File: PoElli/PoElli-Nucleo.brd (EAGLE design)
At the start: 79.5 x 70 mm, 121 parts, among them CN10 NUCLEO-CN10, CN7 NUCLEO-CN7, J3 M022.54MM, J4 M022.54MM, Q3 FDMC2674, Q4 IRFL4310, SW1 A6H2101, SW2 A6H2101, T1 Coilcraft 230NL, T2 FLYBACK750311689, U4 LT3748, U5 TPS2378, U6 ENC424J600, X1 POE-TP-SHIELDED-RJ45-MOLEX-85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, Y1 25 MHz

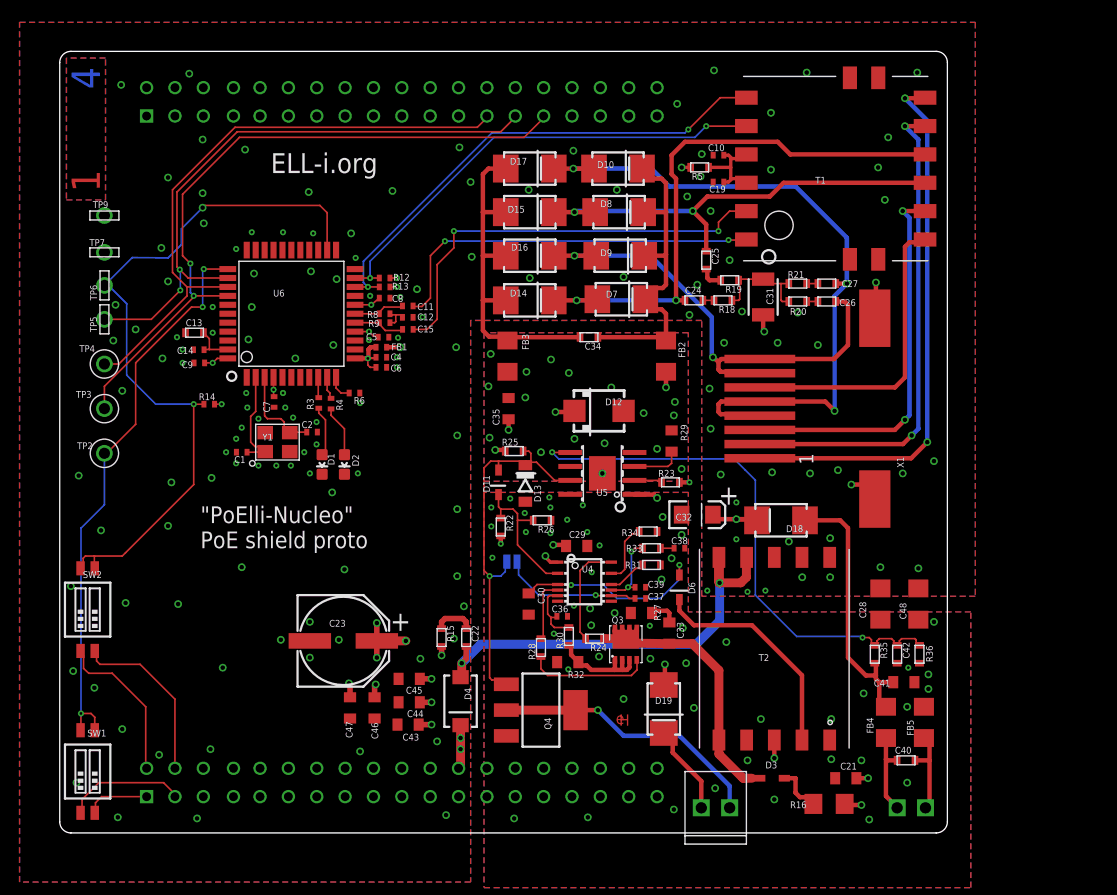
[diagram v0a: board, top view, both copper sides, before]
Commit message: Fix mistakes from first prototype round
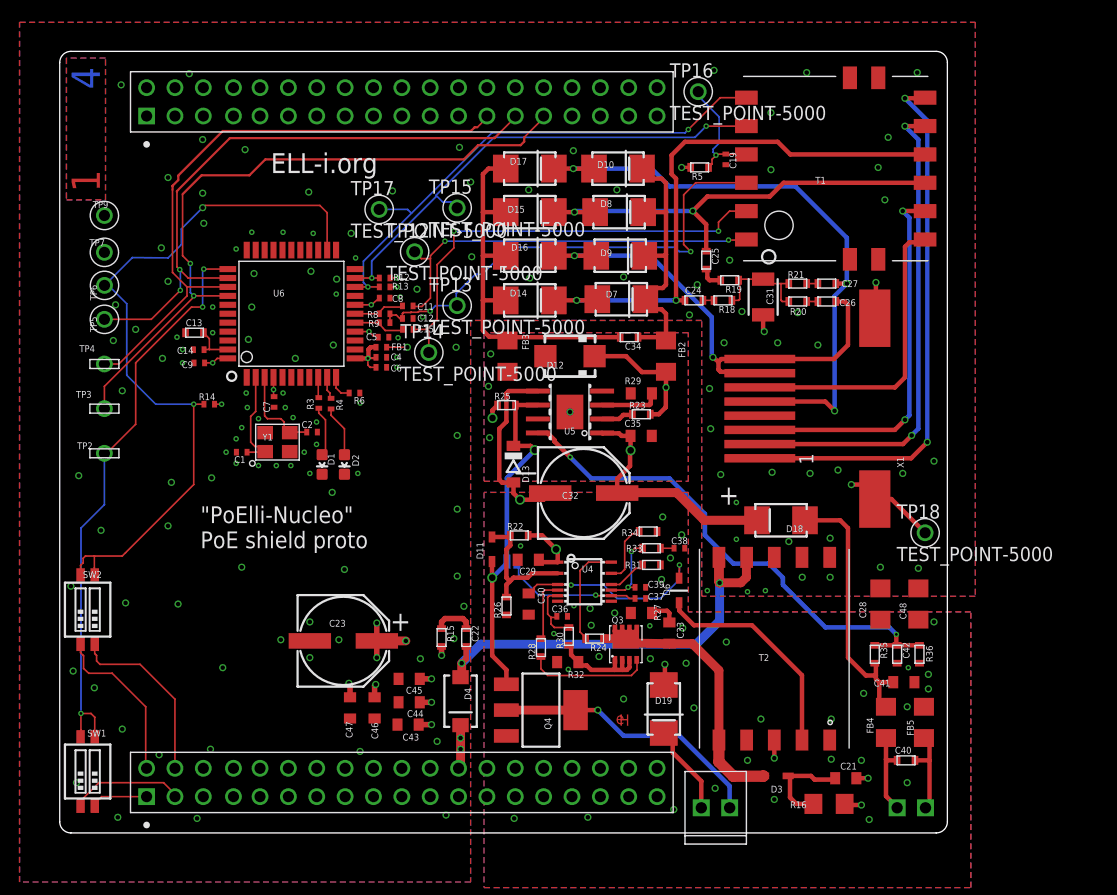
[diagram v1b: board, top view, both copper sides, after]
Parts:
- removed C10: 10nF, ELL-i-Passives:C0402
- added TP12, TP13, TP14, TP15, TP16, TP17, TP18: TEST_POINT-5000, ELL-i-Passives:TP_5000
- C12: value 100nF -> 10nF
- C32: value 47uF -> 10uF 100 V; device ELL-i-Passives:CT3216 -> ELL-i-Passives:CPOL_PANASONIC_E
- CN7: value NUCLEO-CN7 -> NUCLEO-CN10
- TP2, TP3, TP4: device ELL-i-Passives:TP_5000 -> ELL-i-Passives:TP_5021
- TP5, TP6, TP7, TP9: device ELL-i-Passives:TP_5021 -> ELL-i-Passives:TP_5000
- moved C35 12.1 mm to (52.1, 35.6), turned to 0 degrees
- moved C32 10.4 mm to (46.9, 30.4)
- moved R26 8.31 mm to (40.0, 20.3), turned to 90 degrees
- moved R23 6.64 mm to (52.1, 37.5)
- moved U5 6.22 mm to (45.7, 37.7)
- moved D11 6.02 mm to (38.7, 25.4)
- moved D12 5.55 mm to (45.7, 42.7), turned to 180 degrees
- moved R29 5.06 mm to (52.1, 39.4), turned to 0 degrees
- moved C29 4.51 mm to (42.0, 24.5), turned to 180 degrees
- moved R25 4.17 mm to (40.0, 38.3)
- moved C34 3.60 mm to (51.0, 44.4)
- moved C19 2.13 mm to (59.7, 60.3), turned to 90 degrees
- moved D13 2.03 mm to (40.6, 33.0)
- moved R22 1.82 mm to (41.2, 26.6), turned to 0 degrees
- moved D3 0.40 mm to (64.1, 5.11), turned to 180 degrees
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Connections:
- removed net N$44: C12.2, R8.1, R9.1
- new net TPINCT: C12.2, R8.1, R9.1, T1.3, TP13.P$1
- net GNDA: no longer C10.1
- net INTVCC: now also D6.C; no longer D6.2
- net N$28: now also D3.A; no longer D3.1
- net N$29: now also D6.A; no longer D6.1
- net N$33: now also D3.C; no longer D3.2
- net N$40: now also TP16.P$1; no longer C10.2, T1.3
- net N$54: now also U5.8; no longer U5.5
- net RTN: now also C32.-, U5.5; no longer C32.C, U5.8
- net SGND: now also TP18.P$1
- net TPIN+: now also TP14.P$1
- net TPIN-: now also TP12.P$1
- net TPOUT+: now also TP17.P$1
- net TPOUT-: now also TP15.P$1
- net U4_EN: now also D11.A; no longer D11.1
- net U5_CDB: now also D11.C, U5.6; no longer D11.2, U5.7
- net VDD: now also C32.+; no longer C32.A
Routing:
- net TPINCT: track 0.00 -> 43.3 mm, vias 0 -> 2
- net VDD: track 24.6 -> 46.7 mm, vias 14 -> 8
- net RTN: track 0.00 -> 17.0 mm, vias 50 -> 38
- net POE_B+: track 63.4 -> 55.1 mm
- net SGND: track 34.7 -> 40.5 mm
- net N$33: track 4.35 -> 8.73 mm
- net N$8: track 31.7 -> 35.3 mm
- net N$6: track 29.6 -> 26.0 mm
- net N$54: track 49.5 -> 46.2 mm
- net N$28: track 27.7 -> 24.5 mm
- net TPOUT+: track 45.0 -> 48.0 mm
- net U5_CDB: track 35.1 -> 32.3 mm, vias 1 -> 2
- net N$44: track 2.46 -> 0.00 mm
- net N$40: track 8.72 -> 11.1 mm, vias 0 -> 1
- net TPOUT-: track 42.4 -> 44.7 mm
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
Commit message: rev 3 DRC ok
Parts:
- removed TP12, TP13, TP14, TP15, TP16, TP17: TEST_POINT-5000, ELL-i-Passives:TP_5000
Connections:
- net N$40: no longer TP16.P$1
- net TPIN+: no longer TP14.P$1
- net TPIN-: no longer TP12.P$1
- net TPINCT: no longer TP13.P$1
- net TPOUT+: no longer TP17.P$1
- net TPOUT-: no longer TP15.P$1
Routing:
- net POE_B+: track 55.1 -> 61.9 mm
- net N$40: track 11.1 -> 4.28 mm, vias 1 -> 0
- net N$28: track 24.5 -> 29.5 mm
- net TPOUT+: track 48.0 -> 45.0 mm
- net TPOUT-: track 44.7 -> 42.3 mm
- net TPIN+: track 40.6 -> 38.7 mm
- net TPIN-: track 36.3 -> 34.6 mm
- net VDD: track 46.7 -> 47.6 mm
- net TPINCT: track 43.3 -> 42.6 mm

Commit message: rev 0.3
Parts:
- Q3: value FDMC2674 -> FDMC2674HANDSOLDERING; device ELL-i-DIscreteSemi:MLP8L33 -> ELL-i-DIscreteSemi:MLP8L33_HS
- moved C25 2.08 mm to (56.9, 49.5), turned to 0 degrees
- moved Q3 0.44 mm to (50.7, 16.5)
- moved C5 0.21 mm to (28.8, 44.5)
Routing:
- net RTN: track 17.0 -> 94.4 mm, vias 38 -> 11
- net GNDA: track 0.00 -> 48.5 mm, vias 137 -> 24
- net +3V3: track 4.12 -> 34.4 mm, vias 4 -> 3
- net U4_SS: track 12.6 -> 38.9 mm
- net POE_A+: track 50.6 -> 75.1 mm
- net VDD: track 47.6 -> 70.0 mm
- net POE_B+: track 61.9 -> 80.3 mm, vias 3 -> 2
- net POE_A-: track 40.4 -> 52.5 mm
- net VIN: track 16.2 -> 28.3 mm, vias 11 -> 0
- net N$8: track 35.3 -> 25.7 mm
- net UNREG_6V+: track 41.3 -> 33.7 mm
- net N$6: track 26.0 -> 18.7 mm
- net ENC-3V3: track 15.0 -> 21.9 mm, vias 6 -> 5
- net ETH_SS: track 52.5 -> 59.3 mm, vias 3 -> 0
- net SGND: track 40.5 -> 47.0 mm
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- removed copper zone on layer 2, net VSS
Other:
- board text added: "2014-07-21"
- board text added: "PoElli-Nucleo PoE shield proto rev 0.3"
- board text removed: ""PoElli-Nucleo" PoE shield proto"

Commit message: PoElli 0.4 Schema, tentative layout
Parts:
- removed C14: 100nF, ELL-i-Passives:C0402
- removed C23: 220uF, ELL-i-Passives:CPOL_PANASONIC_E
- removed C29: 1uF, ELL-i-Passives:C0805
- removed CN10, CN7: NUCLEO-CN10, ELL-i-Boards:NUCLEO-HEADER
- removed NUCLEO: NUCLEO-SHIELD-OUTLINE-EXTENDED, ELL-i-Boards:NUCLEO-SHIELD-UNDERSIDE-EXTENDED-OUTLINE
- removed R38: OPEN, SparkFun-Passives:SJ_2S-NO
- removed SW1, SW2: A6H2101, SparkFun-Electromechanical:DIPSWITCH-02-50MIL
- removed T2: FLYBACK750311689, ELL-i-Transformers:WE_EP13_SMD_10PIN
- added SJ1, SJ2, SJ3, SJ4: SOLDERJUMPERNO, SparkFun-Passives:SJ_2S-NO
- added U$2: NUCLEO-SHIELD-20PIN, ELL-i-Boards:NUCLEO-SHIELD-UNDERSIDE-SHORT-20-PINHEADER
- C1, C12, C19, C2, C36, C37, C38, C39: device ELL-i-Passives:C0402 -> ELL-i-Passives:SMD0805-A
- C13, C22, C42: device ELL-i-Passives:C0603 -> ELL-i-Passives:SMD0805-A
- C24, C25, C26, C27: value 10nF -> 10nF 100V; device ELL-i-Passives:C0603 -> ELL-i-Passives:SMD0805-A
- C28, C48: value 1nF -> 1nF 2kV
- C30: value 4u7 -> 4u7 25 V; device ELL-i-Passives:C0805 -> ELL-i-Passives:SMD0805-A
- C31: value 1nF -> 1nF 2kV; device ELL-i-Passives:C1210 -> ELL-i-Passives:SMD1206-A
- C32: device ELL-i-Passives:CPOL_PANASONIC_E -> ELL-i-Passives:SMD1206-A
- C33: value 150pF NP -> 150pF 200V NP; device ELL-i-Passives:C0805 -> ELL-i-Passives:SMD0805-A
- C34, C40: value 1nF -> 10nF 100V; device ELL-i-Passives:C0603 -> ELL-i-Passives:SMD0402-B
- C35, C41: value 100nF -> 100nF 100V; device ELL-i-Passives:C0805 -> ELL-i-Passives:SMD0805-A
- C4: value 47pF -> 100nF; device ELL-i-Passives:C0402 -> ELL-i-Passives:SMD0805-A
- C43, C44, C45, C46, C47: device ELL-i-Passives:C0805 -> ELL-i-Passives:SMD1206-A
- C5, C6, C7: value 1nF -> 100nF; device ELL-i-Passives:C0402 -> ELL-i-Passives:SMD0805-A
- C8, C9: device ELL-i-Passives:C0402 -> ELL-i-Passives:SMD0402-B
- D2: value YELLOW -> GREEN
- Q4: value IRFL4310 -> FDMC2674HANDSOLDERING; device ELL-i-DIscreteSemi:SOT223 -> ELL-i-DIscreteSemi:MLP8L33_HS
- R12, R13, R14, R6, R8, R9: device ELL-i-Passives:R0402 -> ELL-i-Passives:SMD0805-A
- R15, R18, R19, R20, R21, R24, R28, R30, R31, R33, R34, R35, R36: device ELL-i-Passives:R0603 -> ELL-i-Passives:SMD0805-A
- R27: device ELL-i-Passives:R0805 -> ELL-i-Passives:SMD0805-A
- R3, R4: value 180 -> 220; device ELL-i-Passives:R0402 -> ELL-i-Passives:SMD0805-A
- U$1: value (none) -> FLYBACK-3_OUTPUTS_749119350; device hapines:EH-LOGO -> ELL-i-Transformers:WE_749119350
- X1: value POE-TP-SHIELDED-RJ45-MOLEX-85502-5008 -> POE-TP-SHIELDED-LEDSTE1888250; device ELL-i-Connectors:MOLEX-85502-5008 -> ELL-i-Connectors:TE1888250
- moved C48 206.8 mm to (-110.5, 108.0), turned to 0 degrees
- moved R36 199.7 mm to (-86.4, 130.8), turned to 0 degrees
- moved C28 199.1 mm to (-105.4, 108.0), turned to 0 degrees
- moved TP18 194.3 mm to (-99.1, 108.0)
- moved C42 191.4 mm to (-80.0, 128.3), turned to 0 degrees
- moved R35 191.3 mm to (-80.0, 130.8), turned to 0 degrees
- moved J4 189.7 mm to (-82.5, 108.0), flipped to the top, turned to 0 degrees
- moved R18 189.2 mm to (-111.8, 128.3), turned to 0 degrees
- moved C41 188.3 mm to (-73.7, 128.3)
- moved C40 187.9 mm to (-67.3, 128.3)
- moved C25 186.8 mm to (-114.3, 124.5)
- moved C24 181.8 mm to (-108.0, 124.5)
- moved J3 172.4 mm to (-76.2, 108.0), turned to 0 degrees
- moved C19 167.7 mm to (-95.2, 124.5), turned to 0 degrees
- moved D3 165.0 mm to (-58.4, 115.6), turned to 0 degrees
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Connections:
- removed net UNREG_6V+: C22.2, D4.A, T2.6, T2.7
- new net TRAFO_OUT: C22.P$2, D4.A, U$1.P$10, U$1.P$11, U$1.P$12
- net +3V3: now also R12.P$2, R13.P$2, U$2.CN7_12, U$2.CN7_16; no longer CN7.12, CN7.16, R12.2, R13.2
- net ENC-3V3: now also C4.P$2, C5.P$2, C6.P$2, C7.P$2, R14.P$2; no longer C4.2, C5.2, C6.2, C7.2, R14.2
- net ETH_INT: now also R14.P$1, SJ1.1, SJ2.1; no longer R14.1, SW2.3, SW2.4
- net ETH_MISO: now also U$2.CN10_27; no longer CN10.27
- net ETH_MOSI: now also U$2.CN10_25; no longer CN10.25
- net ETH_SCK: now also U$2.CN10_29; no longer CN10.29
- net ETH_SS: now also SJ3.1, SJ4.1; no longer SW1.3, SW1.4
- net GNDA: now also C1.P$2, C12.P$1, C13.P$2, C19.P$1, C2.P$2, C4.P$1, C43.P$2, C44.P$2, C45.P$2, C46.P$2, C47.P$2, C5.P$1, C6.P$1, C7.P$1, R6.P$1, U$1.P$7, U$1.P$8, U$1.P$9, U$2.CN7_22; no longer C1.2, C12.1, C13.2, C14.2, C19.1, C2.2, C23.-, C4.1, C43.2, C44.2, C45.2, C46.2, C47.2, C5.1, C6.1, C7.1, CN7.22, R6.1, T2.10, T2.9
- net INTVCC: now also C30.P$1; no longer C30.1
- net N$10: now also Q4.5, Q4.6, Q4.7, Q4.8, Q4.F1; no longer Q4.2, Q4.4
- net N$11: now also SJ3.2, U$2.CN7_1; no longer CN7.1, SW1.2
- net N$12: now also SJ4.2, U$2.CN7_3; no longer CN7.3, SW1.1
- net N$13: now also SJ2.2, U$2.CN7_2; no longer CN7.2, SW2.1
- net N$14: now also SJ1.2, U$2.CN7_4; no longer CN7.4, SW2.2
- net N$15: now also C33.P$2, R27.P$1; no longer C33.2, R27.1
- net N$16: now also C22.P$1, R15.P$1; no longer C22.1, R15.1
- net N$22: now also C39.P$1, R33.P$2; no longer C39.1, R33.2
- net N$23: now also C38.P$1, R33.P$1; no longer C38.1, R33.1
- net N$24: now also R28.P$2; no longer R28.2
- net N$25: now also R28.P$1; no longer R28.1
- net N$26: now also C36.P$1, R30.P$2; no longer C36.1, R30.2
- net N$27: now also R30.P$1; no longer R30.1
- net N$28: now also C33.P$1, R24.P$1, U$1.P$1; no longer C33.1, R24.1, T2.5
- net N$29: now also U$1.P$5; no longer T2.2
- net N$31: now also R24.P$2; no longer R24.2
- net N$32: now also R34.P$2; no longer R34.2
- net N$36: now also R4.P$2; no longer R4.2
- net N$37: now also C1.P$1; no longer C1.1
- net N$38: now also R3.P$1; no longer R3.1
- net N$39: now also R8.P$2; no longer R8.2
- net N$40: now also C19.P$2; no longer C19.2
- net N$41: now also R4.P$1; no longer R4.1
- net N$42: now also R3.P$2; no longer R3.2
- net N$45: now also R6.P$2; no longer R6.2
- net N$47: now also C2.P$1; no longer C2.1
- net N$48: now also C27.P$2, R21.P$2; no longer C27.2, R21.2
- net N$5: now also C31.P$1, R18.P$1, R19.P$1, R20.P$1, R21.P$1; no longer C31.1, R18.1, R19.1, R20.1, R21.1
- net N$50: now also C24.P$2, R18.P$2; no longer C24.2, R18.2
- net N$51: now also C25.P$2, R19.P$2; no longer C25.2, R19.2
- net N$52: now also C26.P$2, R20.P$2; no longer C26.2, R20.2
- net N$54: now also C42.P$1, R35.P$1, R36.P$2; no longer C42.1, R35.1, R36.2
- net N$59: now also R9.P$2; no longer R9.2
- net N$7: now also R31.P$2; no longer R31.2
- net N$76: now also C41.P$1, R35.P$2; no longer C41.1, R35.2
- net POE_A+: now also C24.P$1; no longer C24.1
- net POE_A-: now also C25.P$1; no longer C25.1
- net POE_B+: now also C27.P$1; no longer C27.1
- net POE_B-: now also C26.P$1; no longer C26.1
- net RTN: now also C30.P$2, C32.P$2, C36.P$2, C37.P$2, C38.P$2, C39.P$2, C41.P$2, C42.P$2, Q4.1, Q4.2, R27.P$2, R31.P$1, R34.P$1, R36.P$1, U$1.P$6; no longer C29.2, C30.2, C32.-, C36.2, C37.2, C38.2, C39.2, C41.2, C42.2, R27.2, R31.1, R34.1, R36.1, T2.1
- net SGND: now also C31.P$2, X1.GND@1, X1.GND@2, X1.GND@3, X1.GND@4; no longer C31.2, X1.S1, X1.S2
- net TPINCT: now also C12.P$2, R8.P$1, R9.P$1; no longer C12.2, R8.1, R9.1
- net TPOUT+: now also R13.P$1; no longer R13.1
- net TPOUT-: now also R12.P$1; no longer R12.1
- net U4_SS: now also C37.P$1; no longer C37.1, R38.1
- net U5_CDB: now also Q4.4; no longer Q4.1, R38.2
- net VCAP: now also C13.P$1; no longer C13.1, C14.1
- net VDD: now also C32.P$1, C35.P$1, D12.C, U$1.P$3; no longer C29.1, C32.+, C35.1, D12.1, T2.3
- net VIN: now also C43.P$1, C44.P$1, C45.P$1, C46.P$1, C47.P$1, R15.P$2, U$2.CN7_24; no longer C23.+, C43.1, C44.1, C45.1, C46.1, C47.1, CN7.24, R15.2
- net VSS: now also C35.P$2, D12.A; no longer C35.2, D12.2
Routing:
- net RTN: track 94.4 -> 0.00 mm, vias 11 -> 0
- net POE_B+: track 80.3 -> 0.00 mm, vias 2 -> 0
- net POE_A+: track 75.1 -> 0.00 mm, vias 2 -> 0
- net VDD: track 70.0 -> 0.00 mm, vias 8 -> 0
- net ETH_INT: track 65.8 -> 0.00 mm
- net ETH_SS: track 59.3 -> 0.00 mm
- net ETH_SCK: track 58.3 -> 0.00 mm, vias 1 -> 0
- net POE_A-: track 52.5 -> 0.00 mm, vias 2 -> 0
- net ETH_MOSI: track 51.7 -> 0.00 mm, vias 1 -> 0
- net N$54: track 51.5 -> 0.00 mm, vias 2 -> 0
- net ETH_MISO: track 49.8 -> 0.00 mm, vias 1 -> 0
- net SGND: track 47.0 -> 0.00 mm, vias 3 -> 0
- net POE_B-: track 45.5 -> 0.00 mm, vias 2 -> 0
- net GNDA: track 48.5 -> 3.84 mm, vias 24 -> 0
- net TPINCT: track 39.4 -> 0.00 mm, vias 2 -> 0
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- removed copper zone on layer 15, net +3V3
- removed copper zone on layer 15, net ENC-3V3
- removed copper zone on layer 1, net GNDA
- removed copper zone on layer 16, net GNDA
- removed copper zone on layer 2, net GNDA
- removed copper zone on layer 1, net N$199
- removed copper zone on layer 15, net N$199
- removed copper zone on layer 16, net N$199
- removed copper zone on layer 2, net N$199
- removed copper zone on layer 1, net RTN
- removed copper zone on layer 16, net RTN
- removed copper zone on layer 2, net RTN
- removed copper zone on layer 15, net VDD
- removed copper zone on layer 15, net VIN
- removed copper zone on layer 1, net VSS
- removed copper zone on layer 16, net VSS
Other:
- board size 79.5 x 70 mm -> 160 x 100 mm
- board text removed: "+"
- board text removed: "1"
- board text removed: "2"
- board text removed: "2014-07-21"
- board text removed: "3"
- board text removed: "4"
- board text removed: "ELL-i.org"
- board text removed: "PoElli-Nucleo PoE shield proto rev 0.3"
- board text removed: "https://github.com/Ell-i/ELL-i-Eagle-Boards"

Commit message: tentative layout
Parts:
- removed D10, D14, D15, D16, D17, D7, D8, D9: B2100, ELL-i-DIscreteSemi:DIODE-B2100
- added C10: 1nF 2kV, ELL-i-Passives:SMD1206-A
- added C3: 100nF, ELL-i-Passives:SMD0805-A
- added U$3, U$4: BRIDGE-RECTIFIER, ELL-i-DIscreteSemi:MBS1
- C11, C15: device ELL-i-Passives:C0402 -> ELL-i-Passives:SMD0402-B
- C34: device ELL-i-Passives:SMD0402-B -> ELL-i-Passives:SMD0805-A
- R23, R5: device ELL-i-Passives:R0603 -> ELL-i-Passives:SMD0805-A
- R29: device ELL-i-Passives:R0805 -> ELL-i-Passives:SMD0805-A
- moved R18 211.8 mm to (77.6, 33.5), turned to 90 degrees
- moved C25 208.5 mm to (75.2, 37.5), turned to 270 degrees
- moved C24 204.9 mm to (77.6, 37.5), turned to 270 degrees
- moved J4 203.3 mm to (107.5, 35.5), turned to 270 degrees
- moved J3 195.2 mm to (107.5, 41.7), turned to 270 degrees
- moved C19 190.9 mm to (85.1, 62.0), turned to 270 degrees
- moved D13 177.4 mm to (97.8, 32.8), turned to 270 degrees
- moved FB5 168.4 mm to (101.5, 31.4), turned to 180 degrees
- moved C35 166.5 mm to (95.2, 43.8)
- moved C12 165.7 mm to (70.3, 60.6), turned to 270 degrees
- moved FB4 162.7 mm to (101.4, 33.9), turned to 180 degrees
- moved D12 161.0 mm to (90.9, 31.7), turned to 180 degrees
- moved R29 160.0 mm to (89.5, 39.3)
- moved C31 156.6 mm to (81.5, 31.5)
- moved D18 156.1 mm to (117.5, 44.5), turned to 90 degrees
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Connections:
- new net N$9: C10.P$1, R20.P$1, R21.P$1
- net +3V3: now also R5.P$2; no longer R5.2
- net ENC-3V3: now also C3.P$2
- net GNDA: now also C3.P$1
- net N$18: now also R23.P$1; no longer R23.1
- net N$19: now also R29.P$2; no longer R29.2
- net N$40: now also R5.P$1; no longer R5.1
- net N$5: no longer R20.P$1, R21.P$1
- net N$6: now also C34.P$1, U$3.+, U$4.+; no longer C34.1, D10.C, D7.C, D8.C, D9.C
- net N$8: now also C34.P$2, U$3.-, U$4.-; no longer C34.2, D14.A, D15.A, D16.A, D17.A
- net POE_A+: now also U$3.AC1; no longer D14.C, D7.A
- net POE_A-: now also U$3.AC2; no longer D15.C, D8.A
- net POE_B+: now also U$4.AC1; no longer D10.A, D17.C
- net POE_B-: now also U$4.AC2; no longer D16.C, D9.A
- net SGND: now also C10.P$2
- net VDD: now also R23.P$2; no longer R23.2
- net VSS: now also R29.P$1; no longer R29.1
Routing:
- net POE_B-: track 0.00 -> 33.6 mm
- net POE_B+: track 0.00 -> 19.7 mm
- net TPOUT+: track 18.8 -> 5.02 mm
- net GNDA: track 3.84 -> 15.8 mm
- net TPOUT-: track 12.9 -> 2.18 mm
- net POE_A+: track 0.00 -> 9.43 mm
- net POE_A-: track 0.00 -> 9.00 mm
- net N$59: track 0.00 -> 7.17 mm
- net N$5: track 0.00 -> 6.67 mm
- net N$39: track 0.00 -> 6.49 mm
- net N$9: track 0.00 -> 5.43 mm
- net VIN: track 4.16 -> 0.00 mm
- net TRAFO_OUT: track 4.01 -> 0.00 mm
- net ENC-3V3: track 12.1 -> 15.8 mm
- net N$52: track 0.00 -> 2.08 mm
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
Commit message: Layout, functional blocks placed down
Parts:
- removed U$1: FLYBACK-3_OUTPUTS_749119350, ELL-i-Transformers:WE_749119350
- removed U$3, U$4: BRIDGE-RECTIFIER, ELL-i-DIscreteSemi:MBS1
- added B1, B2: BRIDGE-RECTIFIER, ELL-i-DIscreteSemi:MBS1
- added T2: FLYBACK-3_OUTPUTS_749119350, ELL-i-Transformers:WE_749119350
- C11, C15: device ELL-i-Passives:SMD0402-B -> ELL-i-Passives:SMD0805-A
- C21: device ELL-i-Passives:C0805 -> ELL-i-Passives:SMD0805-A
- C28, C48: device ELL-i-Passives:C1206 -> ELL-i-Passives:SMD1206-A
- C32: device ELL-i-Passives:SMD1206-A -> ELL-i-Passives:SMD2220-REFLOW
- FB1: device ELL-i-Passives:FB0402 -> ELL-i-Passives:SMD0805-A
- FB2, FB3, FB5: device ELL-i-Passives:FB1206 -> ELL-i-Passives:SMD0805-A
- FB4: device ELL-i-Passives:FB1206 -> ELL-i-Passives:SMD0603-A
- R16: device ELL-i-Passives:R1206 -> ELL-i-Passives:SMD1206-A
- R22, R25, R26: device ELL-i-Passives:R0603 -> ELL-i-Passives:SMD0805-A
- R32: device ELL-i-Passives:R0805 -> ELL-i-Passives:SMD0805-A
- moved R36 211.2 mm to (101.5, 34.4)
- moved R35 204.4 mm to (101.5, 36.8)
- moved C42 201.0 mm to (98.3, 35.5), turned to 270 degrees
- moved C41 196.6 mm to (101.7, 39.2), turned to 180 degrees
- moved D11 188.6 mm to (102.9, 49.3), turned to 90 degrees
- moved U4 178.3 mm to (101.5, 50.3), turned to 270 degrees
- moved C37 172.3 mm to (94.5, 41.9), turned to 270 degrees
- moved R28 165.9 mm to (96.5, 49.8), turned to 270 degrees
- moved R32 162.0 mm to (93.7, 49.8), turned to 270 degrees
- moved R26 161.1 mm to (107.7, 49.7), turned to 270 degrees
- moved C28 160.5 mm to (46.1, 55.0)
- moved R24 154.5 mm to (98.9, 54.8)
- moved R25 150.5 mm to (96.1, 45.8)
- moved R22 149.6 mm to (105.4, 49.7), turned to 90 degrees
- moved D19 149.1 mm to (100.4, 42.5)
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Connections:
- removed net N$1: T1.10, X1.2
- removed net N$2: T1.9, X1.1
- removed net N$3: T1.13, X1.3
- removed net N$4: T1.14, X1.6
- new net RX+: T1.14, X1.3
- new net RX-: T1.13, X1.6
- new net TX+: T1.10, X1.1
- new net TX-: T1.9, X1.2
- net +3V3: now also FB1.P$1; no longer FB1.1
- net ENC-3V3: now also FB1.P$2; no longer FB1.2
- net GNDA: now also C28.P$2, C48.P$2, T2.P$7, T2.P$8, T2.P$9; no longer C28.2, C48.2, U$1.P$7, U$1.P$8, U$1.P$9
- net N$27: now also R32.P$1; no longer R32.1
- net N$28: now also T2.P$1; no longer U$1.P$1
- net N$29: now also T2.P$5; no longer U$1.P$5
- net N$33: now also C21.P$2, R16.P$1; no longer C21.2, R16.1
- net N$39: now also C11.P$2; no longer C11.2
- net N$53: now also FB4.P$1; no longer FB4.1
- net N$55: now also FB5.P$1; no longer FB5.1
- net N$59: now also C15.P$2; no longer C15.2
- net N$6: now also B1.+, B2.+, FB2.P$1; no longer FB2.1, U$3.+, U$4.+
- net N$76: now also FB4.P$2; no longer FB4.2
- net N$8: now also B1.-, B2.-, FB3.P$1; no longer FB3.1, U$3.-, U$4.-
- net POE_A+: now also B1.AC1; no longer U$3.AC1
- net POE_A-: now also B1.AC2; no longer U$3.AC2
- net POE_B+: now also B2.AC1; no longer U$4.AC1
- net POE_B-: now also B2.AC2; no longer U$4.AC2
- net RTN: now also C28.P$1, C48.P$1, FB5.P$2, R26.P$1, R32.P$2, T2.P$6; no longer C28.1, C48.1, FB5.2, R26.1, R32.2, U$1.P$6
- net TPIN+: now also C15.P$1, T1.1; no longer C15.1, T1.2
- net TPIN-: now also C11.P$1, T1.2; no longer C11.1, T1.1
- net TPOUT+: now also T1.5; no longer T1.6
- net TPOUT-: now also T1.6; no longer T1.5
- net TRAFO_OUT: now also T2.P$10, T2.P$11, T2.P$12; no longer U$1.P$10, U$1.P$11, U$1.P$12
- net U4_EN: now also R22.P$1, R26.P$2; no longer R22.1, R26.2
- net U5_CDB: now also R25.P$2; no longer R25.2
- net VDD: now also C21.P$1, FB2.P$2, R16.P$2, R22.P$2, R25.P$1, T2.P$3; no longer C21.1, FB2.2, R16.2, R22.2, R25.1, U$1.P$3
- net VSS: now also FB3.P$2; no longer FB3.2
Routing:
- net POE_B-: track 33.6 -> 0.00 mm
- net N$1: track 21.1 -> 0.00 mm
- net N$2: track 21.0 -> 0.00 mm
- net POE_B+: track 19.7 -> 0.00 mm
- net ENC-3V3: track 15.8 -> 0.00 mm
- net GNDA: track 15.8 -> 0.08 mm
- net N$3: track 10.3 -> 0.00 mm
- net N$4: track 10.3 -> 0.00 mm
- net POE_A+: track 9.43 -> 0.00 mm
- net POE_A-: track 9.00 -> 0.00 mm
- net N$59: track 7.17 -> 0.00 mm
- net N$5: track 6.67 -> 0.00 mm
- net N$39: track 6.49 -> 0.00 mm
- net N$9: track 5.43 -> 0.00 mm
- net TPOUT+: track 5.02 -> 0.00 mm
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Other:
- board text added: "+OUT- 48V 0A3"
- board text added: "48V 0A3"
